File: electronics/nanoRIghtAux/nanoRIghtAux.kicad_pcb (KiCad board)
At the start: 2 copper layers, 87.6 x 71.1 mm, 22 parts, among them J1 Conn_MM5451, J10 Conn_EA_GLCD, J11 Conn_MAX7219, J12 Conn_PWRInput, J13 Conn_MAX_Pwr, J2 Conn_HYDA, J3 Conn_HYDB, J4 Conn_FUEL_FR, J5 Conn_FUEL_AL, J6 Conn_MOT_D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

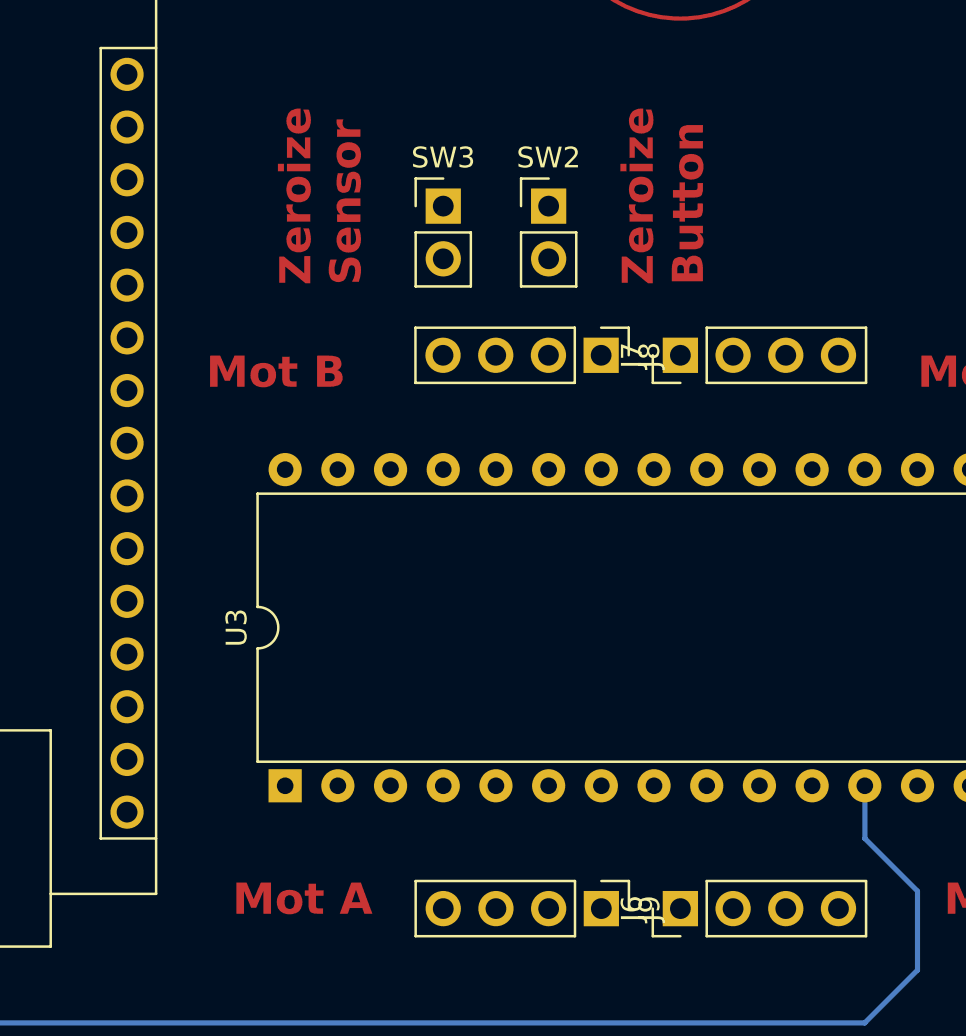
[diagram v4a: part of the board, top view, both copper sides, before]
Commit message: more routing added
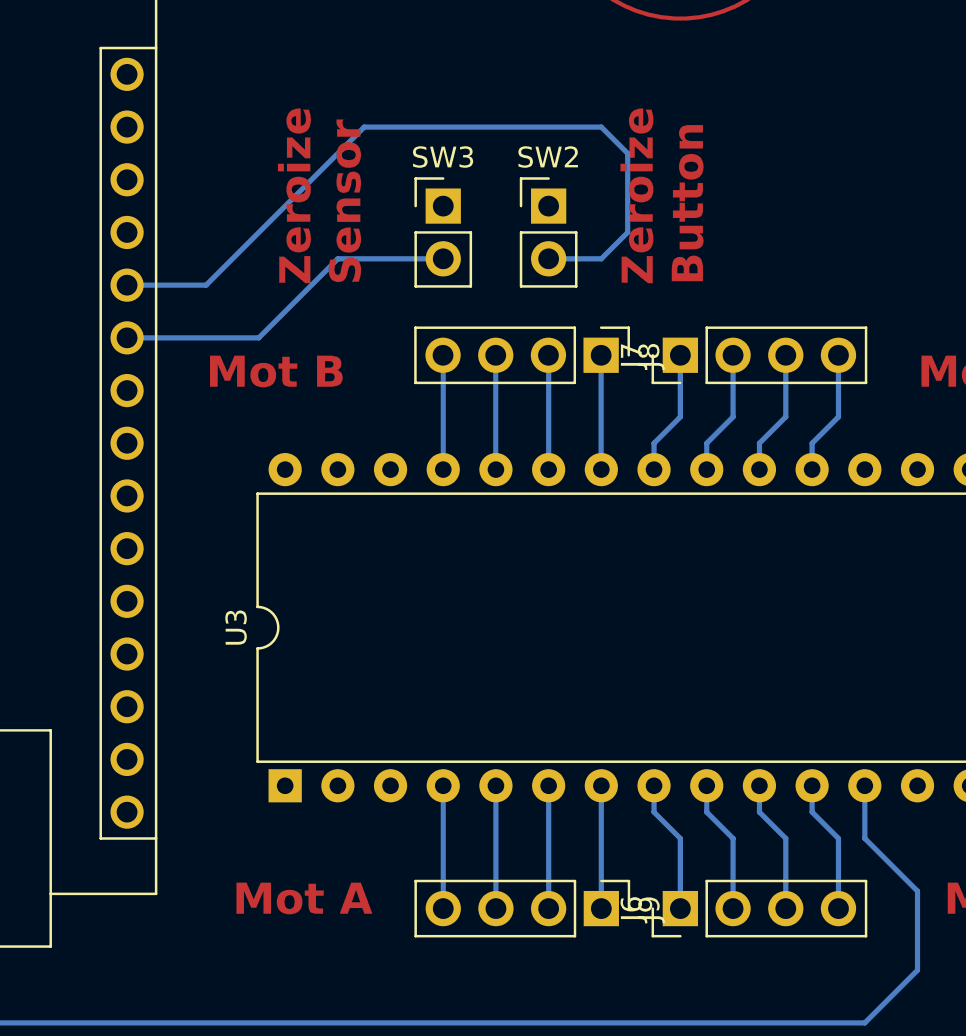
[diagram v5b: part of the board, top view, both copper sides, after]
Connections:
- SW2 pad 2: Net-(A1-A6) -> Net-(A1-A7)
- SW3 pad 2: Net-(A1-A7) -> Net-(A1-A6)
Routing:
- net Net-(A1-A7): track 0.00 -> 36.0 mm
- net Net-(A1-A6): track 0.00 -> 16.8 mm
- net Net-(J6-Pin_4): track 0.00 -> 6.45 mm
- net Net-(J6-Pin_3): track 0.00 -> 6.45 mm
- net Net-(J6-Pin_1): track 0.00 -> 6.45 mm
- net Net-(J6-Pin_2): track 0.00 -> 6.45 mm
- net Net-(J7-Pin_4): track 0.00 -> 6.04 mm
- net Net-(J7-Pin_3): track 0.00 -> 6.04 mm
- net Net-(J7-Pin_1): track 0.00 -> 6.04 mm
- net Net-(J7-Pin_2): track 0.00 -> 6.04 mm
- net Net-(J9-Pin_4): track 0.00 -> 5.92 mm
- net Net-(J9-Pin_3): track 0.00 -> 5.92 mm
- net Net-(J9-Pin_2): track 0.00 -> 5.92 mm
- net Net-(J9-Pin_1): track 0.00 -> 5.92 mm
- net Net-(J8-Pin_3): track 0.00 -> 5.51 mm
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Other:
- board text removed: "RightAUX Control Board"
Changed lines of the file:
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@@
     (pad_to_mask_clearance 0)
     (pcbplotparams
-      (layerselection 0x0000000_fffffffe)
+      (layerselection 0x0000000_7fffffff)
       (plot_on_all_layers_selection 0x0000000_00000000)
       (disableapertmacros false)
@@
       (drillshape 0)
       (scaleselection 1)
-      (outputdirectory "/media/michi/miWorkdata/myproject/F-16SimulatorParts/BMSAIT-RightAux/electronics/nanoRIghtAux/")
+      (outputdirectory "gerber/")
     )
   )
@@
       (net 4 "GND") (pinfunction "1") (pintype "passive"))
     (pad "2" thru_hole oval (at 0 2.54) (size 1.7 1.7) (drill 1) (layers "*.Cu" "*.Mask")
-      (net 23 "Net-(A1-A6)") (pinfunction "2") (pintype "passive"))
+      (net 24 "Net-(A1-A7)") (pinfunction "2") (pintype "passive"))
     (model "${KICAD6_3DMODEL_DIR}/Connector_PinHeader_2.54mm.3dshapes/PinHeader_1x02_P2.54mm_Vertical.wrl"
       (offset (xyz 0 0 0))
@@
       (net 4 "GND") (pinfunction "1") (pintype "passive"))
     (pad "2" thru_hole oval (at 0 2.54) (size 1.7 1.7) (drill 1) (layers "*.Cu" "*.Mask")
-      (net 24 "Net-(A1-A7)") (pinfunction "2") (pintype "passive"))
+      (net 23 "Net-(A1-A6)") (pinfunction "2") (pintype "passive"))
     (model "${KICAD6_3DMODEL_DIR}/Connector_PinHeader_2.54mm.3dshapes/PinHeader_1x02_P2.54mm_Vertical.wrl"
       (offset (xyz 0 0 0))
@@
   (gr_text "Mot B" (at 177.8 92.71) (layer "F.Cu")
     (effects (font (size 1.5 1.5) (thickness 0.3) bold) (justify left bottom))
-  )
-  (gr_text "RightAUX Control Board" (at 196.85 127) (layer "B.SilkS")
-    (effects (font (size 2 2) (thickness 0.15)) (justify left bottom mirror))
   )
   (segment (start 162.56 74.93) (end 165.1 77.47) (width 0.25) (layer "B.Cu") (net 3))
@@
   (segment (start 152.4 113.03) (end 158.75 113.03) (width 0.25) (layer "B.Cu") (net 15))
   (segment (start 151.115 114.315) (end 152.4 113.03) (width 0.25) (layer "B.Cu") (net 15))
+  (segment (start 173.99 90.17) (end 180.34 90.17) (width 0.25) (layer "B.Cu") (net 23))
+  (segment (start 184.15 86.36) (end 189.23 86.36) (width 0.25) (layer "B.Cu") (net 23))
+  (segment (start 180.34 90.17) (end 184.15 86.36) (width 0.25) (layer "B.Cu") (net 23))
+  (segment (start 196.85 86.36) (end 194.31 86.36) (width 0.25) (layer "B.Cu") (net 24))
+  (segment (start 185.42 80.01) (end 196.85 80.01) (width 0.25) (layer "B.Cu") (net 24))
+  (segment (start 198.12 81.28) (end 198.12 85.09) (width 0.25) (layer "B.Cu") (net 24))
+  (segment (start 177.8 87.63) (end 185.42 80.01) (width 0.25) (layer "B.Cu") (net 24))
+  (segment (start 198.12 85.09) (end 196.85 86.36) (width 0.25) (layer "B.Cu") (net 24))
+  (segment (start 196.85 80.01) (end 198.12 81.28) (width 0.25) (layer "B.Cu") (net 24))
+  (segment (start 173.99 87.63) (end 177.8 87.63) (width 0.25) (layer "B.Cu") (net 24))
   (segment (start 144.765 105.41) (end 144.765 81.275) (width 0.25) (layer "B.Cu") (net 28))
   (segment (start 143.51 118.11) (end 143.51 109.22) (width 0.25) (layer "B.Cu") (net 28))
@@
   (segment (start 144.78 119.38) (end 143.51 118.11) (width 0.25) (layer "B.Cu") (net 28))
   (segment (start 143.51 107.95) (end 144.765 106.695) (width 0.25) (layer "B.Cu") (net 28))
+  (segment (start 199.39 111.76) (end 199.39 113.03) (width 0.25) (layer "B.Cu") (net 29))
+  (segment (start 199.39 113.03) (end 200.66 114.3) (width 0.25) (layer "B.Cu") (net 29))
+  (segment (start 200.66 114.3) (end 200.66 117.68) (width 0.25) (layer "B.Cu") (net 29))
+  (segment (start 203.2 114.3) (end 203.2 117.68) (width 0.25) (layer "B.Cu") (net 30))
+  (segment (start 201.93 113.03) (end 203.2 114.3) (width 0.25) (layer "B.Cu") (net 30))
+  (segment (start 201.93 111.76) (end 201.93 113.03) (width 0.25) (layer "B.Cu") (net 30))
+  (segment (start 204.47 113.03) (end 205.74 114.3) (width 0.25) (layer "B.Cu") (net 31))
+  (segment (start 205.74 114.3) (end 205.74 117.68) (width 0.25) (layer "B.Cu") (net 31))
+  (segment (start 204.47 111.76) (end 204.47 113.03) (width 0.25) (layer "B.Cu") (net 31))
+  (segment (start 208.28 114.3) (end 208.28 117.68) (width 0.25) (layer "B.Cu") (net 32))
+  (segment (start 207.01 113.03) (end 208.28 114.3) (width 0.25) (layer "B.Cu") (net 32))
+  (segment (start 207.01 111.76) (end 207.01 113.03) (width 0.25) (layer "B.Cu") (net 32))
+  (segment (start 200.66 93.98) (end 200.66 91.01) (width 0.25) (layer "B.Cu") (net 33))
+  (segment (start 199.39 95.25) (end 200.66 93.98) (width 0.25) (layer "B.Cu") (net 33))
+  (segment (start 199.39 96.52) (end 199.39 95.25) (width 0.25) (layer "B.Cu") (net 33))
+  (segment (start 201.93 95.25) (end 203.2 93.98) (width 0.25) (layer "B.Cu") (net 34))
+  (segment (start 201.93 96.52) (end 201.93 95.25) (width 0.25) (layer "B.Cu") (net 34))
+  (segment (start 203.2 93.98) (end 203.2 91.01) (width 0.25) (layer "B.Cu") (net 34))
+  (segment (start 205.74 93.98) (end 205.74 91.01) (width 0.25) (layer "B.Cu") (net 35))
+  (segment (start 204.47 95.25) (end 205.74 93.98) (width 0.25) (layer "B.Cu") (net 35))
+  (segment (start 204.47 96.52) (end 204.47 95.25) (width 0.25) (layer "B.Cu") (net 35))
+  (segment (start 208.28 93.98) (end 208.28 91.01) (width 0.25) (layer "B.Cu") (net 36))
+  (segment (start 207.01 95.25) (end 208.28 93.98) (width 0.25) (layer "B.Cu") (net 36))
+  (segment (start 207.01 96.52) (end 207.01 95.25) (width 0.25) (layer "B.Cu") (net 36))
+  (segment (start 196.84 96.51) (end 196.85 96.52) (width 0.25) (layer "B.Cu") (net 37))
+  (segment (start 196.84 91.01) (end 196.84 96.51) (width 0.25) (layer "B.Cu") (net 37))
+  (segment (start 194.31 96.52) (end 194.31 91.02) (width 0.25) (layer "B.Cu") (net 38))
+  (segment (start 194.31 91.02) (end 194.3 91.01) (width 0.25) (layer "B.Cu") (net 38))
+  (segment (start 191.76 91.01) (end 191.76 96.51) (width 0.25) (layer "B.Cu") (net 39))
+  (segment (start 191.76 96.51) (end 191.77 96.52) (width 0.25) (layer "B.Cu") (net 39))
+  (segment (start 189.23 91.02) (end 189.22 91.01) (width 0.25) (layer "B.Cu") (net 40))
+  (segment (start 189.23 96.52) (end 189.23 91.02) (width 0.25) (layer "B.Cu") (net 40))
+  (segment (start 196.85 117.68) (end 196.85 111.76) (width 0.25) (layer "B.Cu") (net 41))
+  (segment (start 194.31 111.76) (end 194.31 117.68) (width 0.25) (layer "B.Cu") (net 42))
+  (segment (start 191.77 117.68) (end 191.77 111.76) (width 0.25) (layer "B.Cu") (net 43))
+  (segment (start 189.23 111.76) (end 189.23 117.68) (width 0.25) (layer "B.Cu") (net 44))
   (zone (net 4) (net_name "GND") (layer "B.Cu") (hatch edge 0.5)
     (connect_pads (clearance 0.5))

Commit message: routing done
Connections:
- U3 pad 27: Net-(A1-A4) -> Net-(A1-A5)
- U3 pad 28: Net-(A1-A5) -> Net-(A1-A4)
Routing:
- net Net-(A1-A2): track 0.00 -> 48.4 mm
- net Net-(A1-A1): track 0.00 -> 43.3 mm
- net Net-(A1-A3): track 0.00 -> 16.8 mm
- net Net-(A1-D13): track 0.00 -> 15.0 mm
- net Net-(A1-A0): track 0.00 -> 13.5 mm
- net Net-(A1-A5): track 0.00 -> 13.2 mm
- net Net-(A1-A4): track 0.00 -> 8.15 mm
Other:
- board text added: "MotB"
- board text removed: "Mot B"
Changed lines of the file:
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@@
       (net 20 "Net-(A1-A3)") (pinfunction "Reset") (pintype "input"))
     (pad "27" thru_hole oval (at 15.24 2.54 90) (size 1.6 1.6) (drill 0.8) (layers "*.Cu" "*.Mask")
-      (net 21 "Net-(A1-A4)") (pinfunction "Dir_A") (pintype "input"))
+      (net 22 "Net-(A1-A5)") (pinfunction "Dir_A") (pintype "input"))
     (pad "28" thru_hole oval (at 15.24 0 90) (size 1.6 1.6) (drill 0.8) (layers "*.Cu" "*.Mask")
-      (net 22 "Net-(A1-A5)") (pinfunction "Step_A") (pintype "input"))
+      (net 21 "Net-(A1-A4)") (pinfunction "Step_A") (pintype "input"))
     (model "${KICAD6_3DMODEL_DIR}/Package_DIP.3dshapes/DIP-28_W15.24mm.wrl"
       (offset (xyz 0 0 0))
@@
     (effects (font (size 1.5 1.5) (thickness 0.3) bold) (justify left bottom))
   )
-  (gr_text "Zeroize\nSensor" (at 185.42 87.63 90) (layer "F.Cu")
+  (gr_text "Zeroize\nSensor" (at 189.23 78.74 90) (layer "F.Cu")
     (effects (font (size 1.5 1.5) (thickness 0.3) bold) (justify left bottom))
   )
@@
     (effects (font (size 1 1) (thickness 0.15)) (justify left bottom))
   )
-  (gr_text "Zeroize\nButton" (at 201.93 87.63 90) (layer "F.Cu")
+  (gr_text "Zeroize\nButton" (at 203.2 87.63 90) (layer "F.Cu")
     (effects (font (size 1.5 1.5) (thickness 0.3) bold) (justify left bottom))
   )
@@
     (effects (font (size 1.5 1.5) (thickness 0.3) bold) (justify left bottom))
   )
-  (gr_text "MAX\n7219" (at 138.43 116.84) (layer "F.Cu")
+  (gr_text "MAX\n7219" (at 135.89 116.84) (layer "F.Cu")
     (effects (font (size 1.5 1.5) (thickness 0.3) bold) (justify left bottom))
   )
-  (gr_text "Mot B" (at 177.8 92.71) (layer "F.Cu")
-    (effects (font (size 1.5 1.5) (thickness 0.3) bold) (justify left bottom))
+  (gr_text "MotB" (at 181.61 91.44) (layer "F.Cu")
+    (effects (font (size 1.2 1.2) (thickness 0.3) bold) (justify left bottom))
   )
   (segment (start 162.56 74.93) (end 165.1 77.47) (width 0.25) (layer "B.Cu") (net 3))
@@
   (segment (start 152.4 113.03) (end 158.75 113.03) (width 0.25) (layer "B.Cu") (net 15))
   (segment (start 151.115 114.315) (end 152.4 113.03) (width 0.25) (layer "B.Cu") (net 15))
+  (segment (start 175.26 105.41) (end 179.07 109.22) (width 0.25) (layer "B.Cu") (net 18))
+  (segment (start 179.07 109.22) (end 182.88 109.22) (width 0.25) (layer "B.Cu") (net 18))
+  (segment (start 184.15 110.49) (end 184.15 111.76) (width 0.25) (layer "B.Cu") (net 18))
+  (segment (start 182.88 109.22) (end 184.15 110.49) (width 0.25) (layer "B.Cu") (net 18))
+  (segment (start 173.99 105.41) (end 175.26 105.41) (width 0.25) (layer "B.Cu") (net 18))
+  (segment (start 176.53 102.87) (end 180.34 106.68) (width 0.25) (layer "B.Cu") (net 19))
+  (segment (start 180.34 106.68) (end 209.55 106.68) (width 0.25) (layer "B.Cu") (net 19))
+  (segment (start 209.55 106.68) (end 212.09 109.22) (width 0.25) (layer "B.Cu") (net 19))
+  (segment (start 173.99 102.87) (end 176.53 102.87) (width 0.25) (layer "B.Cu") (net 19))
+  (segment (start 212.09 109.22) (end 212.09 111.76) (width 0.25) (layer "B.Cu") (net 19))
+  (segment (start 186.69 99.06) (end 186.69 96.52) (width 0.25) (layer "B.Cu") (net 20))
+  (segment (start 173.99 97.79) (end 179.07 97.79) (width 0.25) (layer "B.Cu") (net 20))
+  (segment (start 179.07 97.79) (end 181.61 100.33) (width 0.25) (layer "B.Cu") (net 20))
+  (segment (start 185.42 100.33) (end 186.69 99.06) (width 0.25) (layer "B.Cu") (net 20))
+  (segment (start 181.61 100.33) (end 185.42 100.33) (width 0.25) (layer "B.Cu") (net 20))
+  (segment (start 173.99 95.25) (end 180.34 95.25) (width 0.25) (layer "B.Cu") (net 21))
+  (segment (start 180.34 95.25) (end 181.61 96.52) (width 0.25) (layer "B.Cu") (net 21))
+  (segment (start 184.15 93.98) (end 184.15 96.52) (width 0.25) (layer "B.Cu") (net 22))
+  (segment (start 182.88 92.71) (end 184.15 93.98) (width 0.25) (layer "B.Cu") (net 22))
+  (segment (start 173.99 92.71) (end 182.88 92.71) (width 0.25) (layer "B.Cu") (net 22))
   (segment (start 173.99 90.17) (end 180.34 90.17) (width 0.25) (layer "B.Cu") (net 23))
   (segment (start 184.15 86.36) (end 189.23 86.36) (width 0.25) (layer "B.Cu") (net 23))
@@
   (segment (start 191.77 117.68) (end 191.77 111.76) (width 0.25) (layer "B.Cu") (net 43))
   (segment (start 189.23 111.76) (end 189.23 117.68) (width 0.25) (layer "B.Cu") (net 44))
+  (segment (start 175.26 114.3) (end 185.42 114.3) (width 0.25) (layer "B.Cu") (net 47))
+  (segment (start 185.42 114.3) (end 186.69 113.03) (width 0.25) (layer "B.Cu") (net 47))
+  (segment (start 186.69 113.03) (end 186.69 111.76) (width 0.25) (layer "B.Cu") (net 47))
+  (segment (start 173.99 113.03) (end 175.26 114.3) (width 0.25) (layer "B.Cu") (net 47))
+  (segment (start 173.99 100.33) (end 177.8 100.33) (width 0.25) (layer "B.Cu") (net 48))
+  (segment (start 177.8 100.33) (end 181.61 104.14) (width 0.25) (layer "B.Cu") (net 48))
+  (segment (start 181.61 104.14) (end 212.09 104.14) (width 0.25) (layer "B.Cu") (net 48))
+  (segment (start 214.63 106.68) (end 214.63 111.76) (width 0.25) (layer "B.Cu") (net 48))
+  (segment (start 212.09 104.14) (end 214.63 106.68) (width 0.25) (layer "B.Cu") (net 48))
   (zone (net 4) (net_name "GND") (layer "B.Cu") (hatch edge 0.5)
     (connect_pads (clearance 0.5))

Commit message: first routing finished, exported Gerbers/Drillfiles
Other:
- board size 87.6 x 71.1 mm -> 85.1 x 68.6 mm
